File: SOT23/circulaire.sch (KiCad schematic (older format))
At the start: 37 parts, among them J101 Conn_Coaxial, J102 Conn_01x03, U101 LT3042xMSE, U102 LT3093xMSE, U103 OPA847xDBV

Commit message: add ohwr-texts
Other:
- note added: "Copyright Anders E E Wallin, 2020.\nThis documentation describes Open Hardware and is licensed under the\nCERN OHL v. 1.2.\nYou may redistribute and modify this documentation under the terms of the\nCERN OHL v.1.2. (http://ohwr.org/cernohl). This documentation is distributed\nWITHOUT ANY EXPRESS OR IMPLIED WARRANTY, INCLUDING OF\nMERCHANTABILITY, SATISFACTORY QUALITY AND FITNESS FOR A\nPARTICULAR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"
- note added: "MAX +/-20 V DC input"
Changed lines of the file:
@@
 encoding utf-8
 Sheet 1 1
-Title "1\" Photodiode Transimpedance Amplifier"
+Title "1\" Photodiode Transimpedance Amplifier - SOT23"
 Date "2019-12-20"
 Rev "draft"
@@
 	5250 1850 5250 2200
 Connection ~ 5250 2200
+Text Notes 7950 1400 0    50   ~ 0
+Copyright Anders E E Wallin, 2020.\nThis documentation describes Open Hardware and is licensed under the\nCERN OHL v. 1.2.\nYou may redistribute and modify this documentation under the terms of the\nCERN OHL v.1.2. (http://ohwr.org/cernohl). This documentation is distributed\nWITHOUT ANY EXPRESS OR IMPLIED WARRANTY, INCLUDING OF\nMERCHANTABILITY, SATISFACTORY QUALITY AND FITNESS FOR A\nPARTICULAR PURPOSE. Please see the CERN OHL v.1.2 for applicable\nconditions\n
+Wire Notes Line
+	7900 650  11000 650
+Wire Notes Line
+	11000 650  11000 1450
+Wire Notes Line
+	11000 1450 7900 1450
+Wire Notes Line
+	7900 1450 7900 650
+Text Notes 600  5200 0    50   ~ 0
+MAX +/-20 V DC input
 $EndSCHEMATC

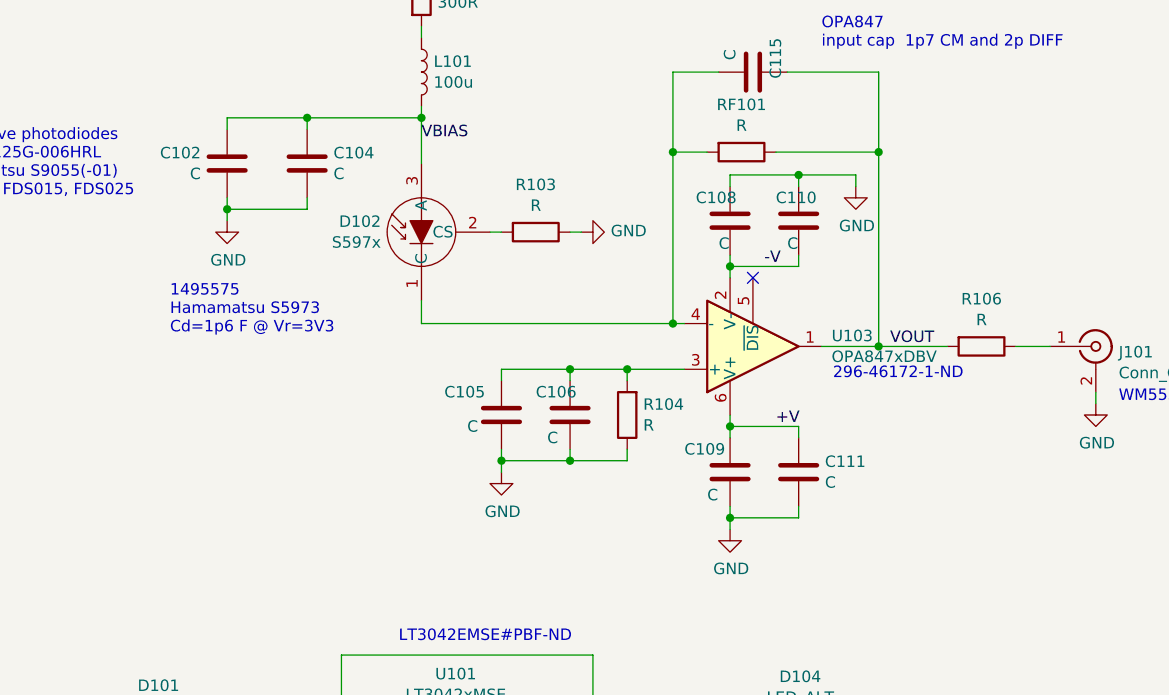
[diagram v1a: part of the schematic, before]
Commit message: add component values
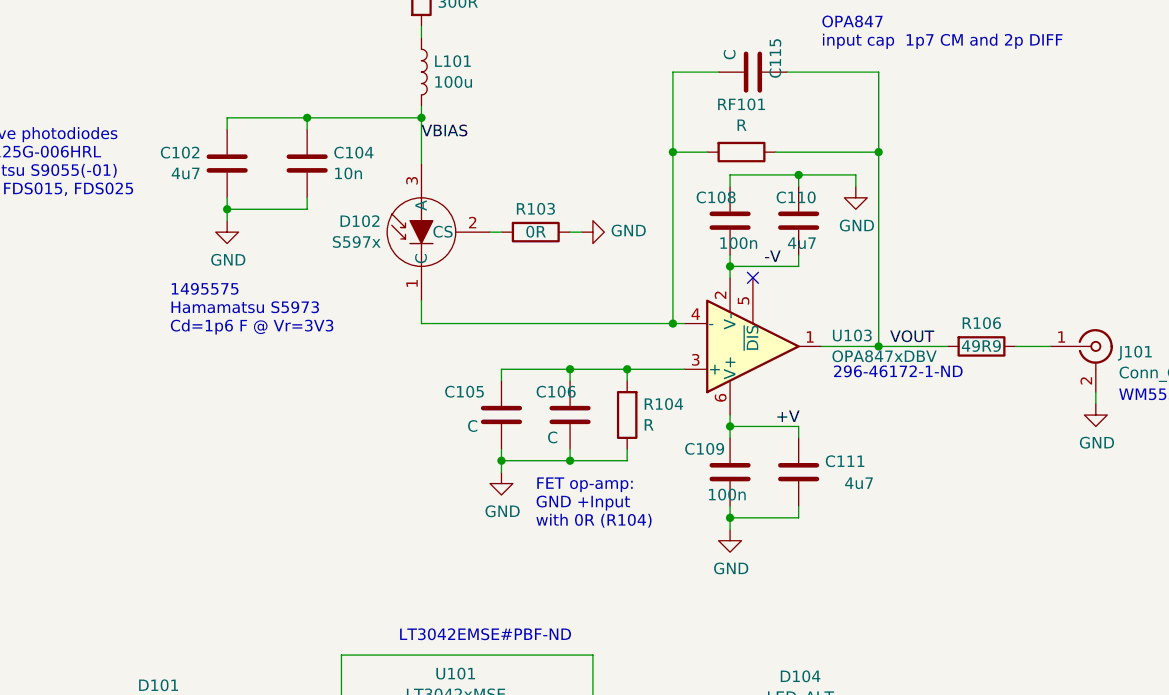
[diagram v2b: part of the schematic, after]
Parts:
- C102, C110, C111: value C -> 4u7
- C104: value C -> 10n
- C108, C109: value C -> 100n
- R103: value R -> 0R
- R106: value R -> 49R9
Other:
- note added: "FET op-amp: \nGND +Input \nwith 0R (R104)"
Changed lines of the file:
@@
 U 1 1 5E080F1F
 P 3750 2550
-F 0 "R103" V 3543 2550 50  0000 C CNN
-F 1 "R" V 3634 2550 50  0000 C CNN
+F 0 "R103" V 3650 2550 50  0000 C CNN
+F 1 "0R" V 3750 2550 50  0000 C CNN
 F 2 "Resistor_SMD:R_0603_1608Metric" V 3680 2550 50  0001 C CNN
 F 3 "~" H 3750 2550 50  0001 C CNN
@@
 U 1 1 5E0831FD
 P 5700 3050
-F 0 "R106" V 5493 3050 50  0000 C CNN
-F 1 "R" V 5584 3050 50  0000 C CNN
+F 0 "R106" V 5600 3050 50  0000 C CNN
+F 1 "49R9" V 5700 3050 50  0000 C CNN
 F 2 "Resistor_SMD:R_0603_1608Metric" V 5630 3050 50  0001 C CNN
 F 3 "~" H 5700 3050 50  0001 C CNN
@@
 P 4600 3600
 F 0 "C109" H 4400 3700 50  0000 L CNN
-F 1 "C" H 4500 3500 50  0000 L CNN
+F 1 "100n" H 4500 3500 50  0000 L CNN
 F 2 "Capacitor_SMD:C_0603_1608Metric" H 4638 3450 50  0001 C CNN
 F 3 "~" H 4600 3600 50  0001 C CNN
@@
 P 4900 3600
 F 0 "C111" H 5015 3646 50  0000 L CNN
-F 1 "C" H 5015 3555 50  0000 L CNN
+F 1 "4u7" H 5100 3550 50  0000 L CNN
 F 2 "Capacitor_SMD:C_0603_1608Metric" H 4938 3450 50  0001 C CNN
 F 3 "~" H 4900 3600 50  0001 C CNN
@@
 P 4600 2500
 F 0 "C108" H 4450 2600 50  0000 L CNN
-F 1 "C" H 4550 2400 50  0000 L CNN
+F 1 "100n" H 4550 2400 50  0000 L CNN
 F 2 "Capacitor_SMD:C_0603_1608Metric" H 4638 2350 50  0001 C CNN
 F 3 "~" H 4600 2500 50  0001 C CNN
@@
 P 4900 2500
 F 0 "C110" H 4800 2600 50  0000 L CNN
-F 1 "C" H 4850 2400 50  0000 L CNN
+F 1 "4u7" H 4850 2400 50  0000 L CNN
 F 2 "Capacitor_SMD:C_0603_1608Metric" H 4938 2350 50  0001 C CNN
 F 3 "~" H 4900 2500 50  0001 C CNN
@@
 P 2750 2250
 F 0 "C104" H 2865 2296 50  0000 L CNN
-F 1 "C" H 2865 2205 50  0000 L CNN
+F 1 "10n" H 2865 2205 50  0000 L CNN
 F 2 "Capacitor_SMD:C_0603_1608Metric" H 2788 2100 50  0001 C CNN
 F 3 "~" H 2750 2250 50  0001 C CNN
@@
 P 2400 2250
 F 0 "C102" H 2515 2296 50  0000 L CNN
-F 1 "C" H 2515 2205 50  0000 L CNN
+F 1 "4u7" H 2515 2205 50  0000 L CNN
 F 2 "Capacitor_SMD:C_0603_1608Metric" H 2438 2100 50  0001 C CNN
 F 3 "~" H 2400 2250 50  0001 C CNN
@@
 Text Notes 600  5200 0    50   ~ 0
 MAX +/-20 V DC input
+Text Notes 3750 3850 0    50   ~ 0
+FET op-amp: \nGND +Input \nwith 0R (R104)
 $EndSCHEMATC
